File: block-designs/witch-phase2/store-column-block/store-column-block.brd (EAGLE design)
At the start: 27.9 x 27.9 mm, 12 parts, among them IC1 74HC125D

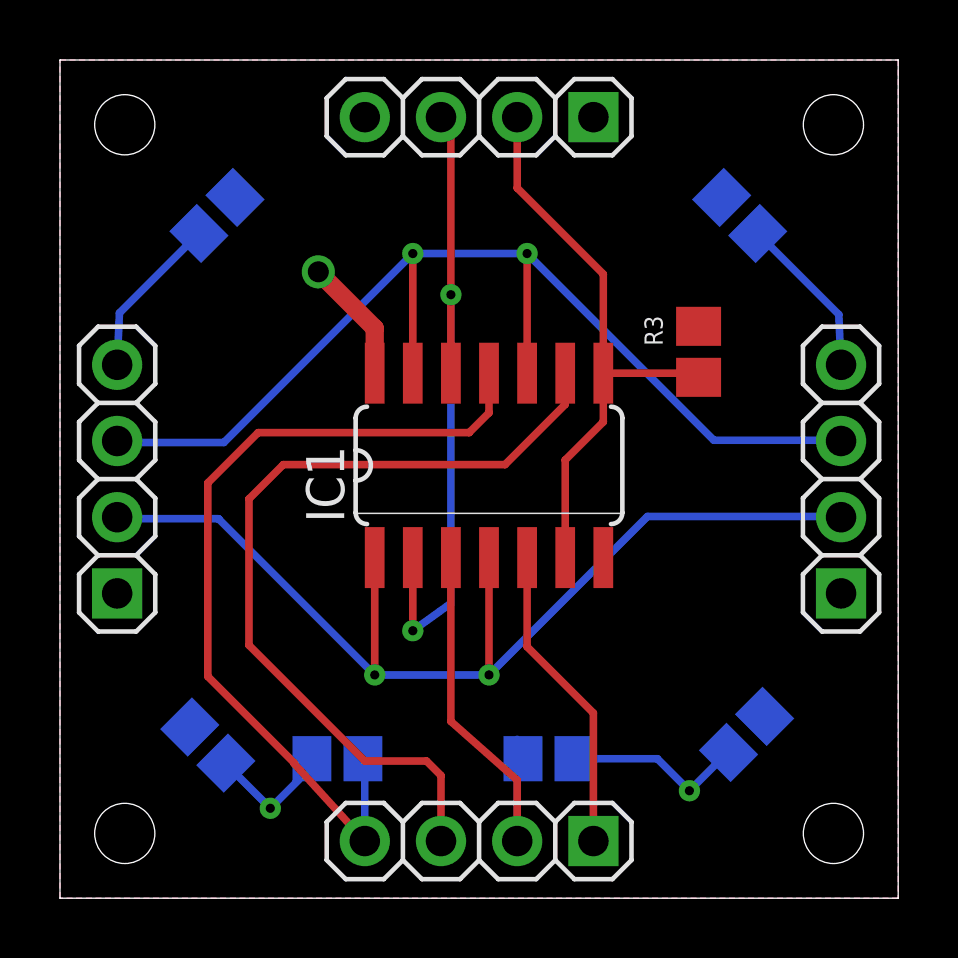
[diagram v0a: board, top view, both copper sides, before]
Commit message: adjust borders for ground/vcc plains and size to match 1.1inch grids
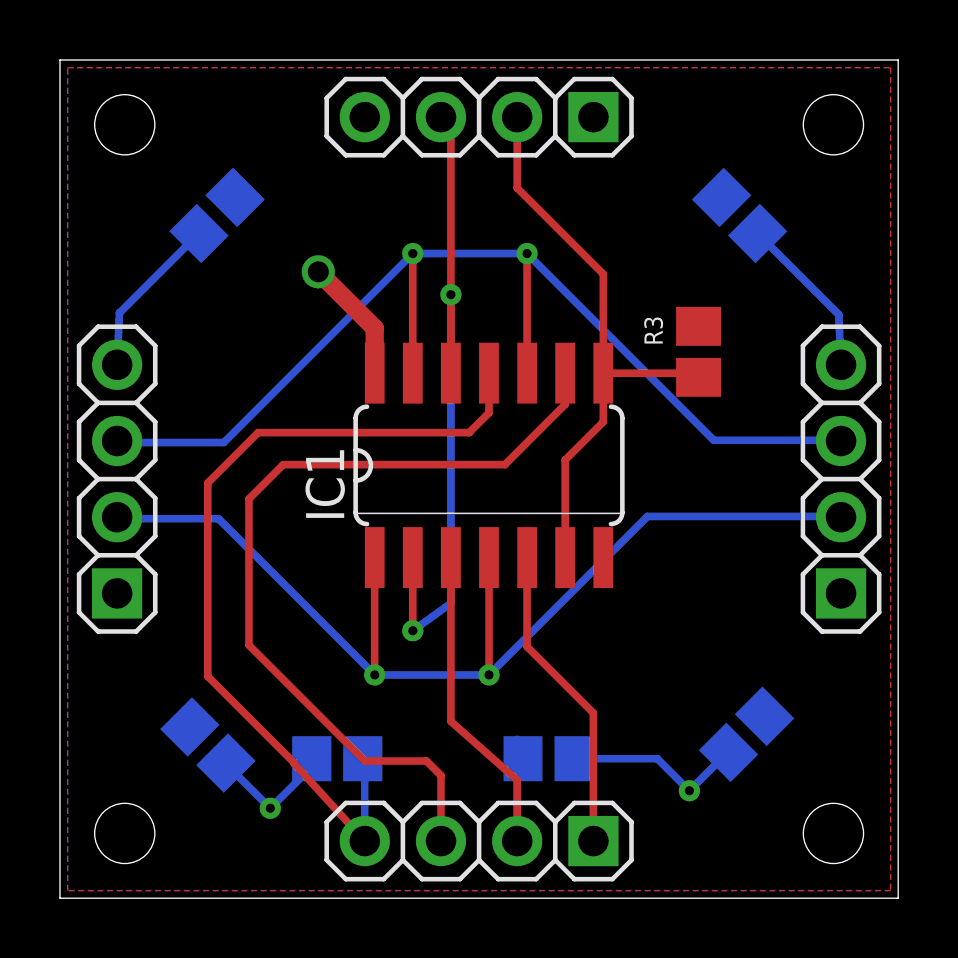
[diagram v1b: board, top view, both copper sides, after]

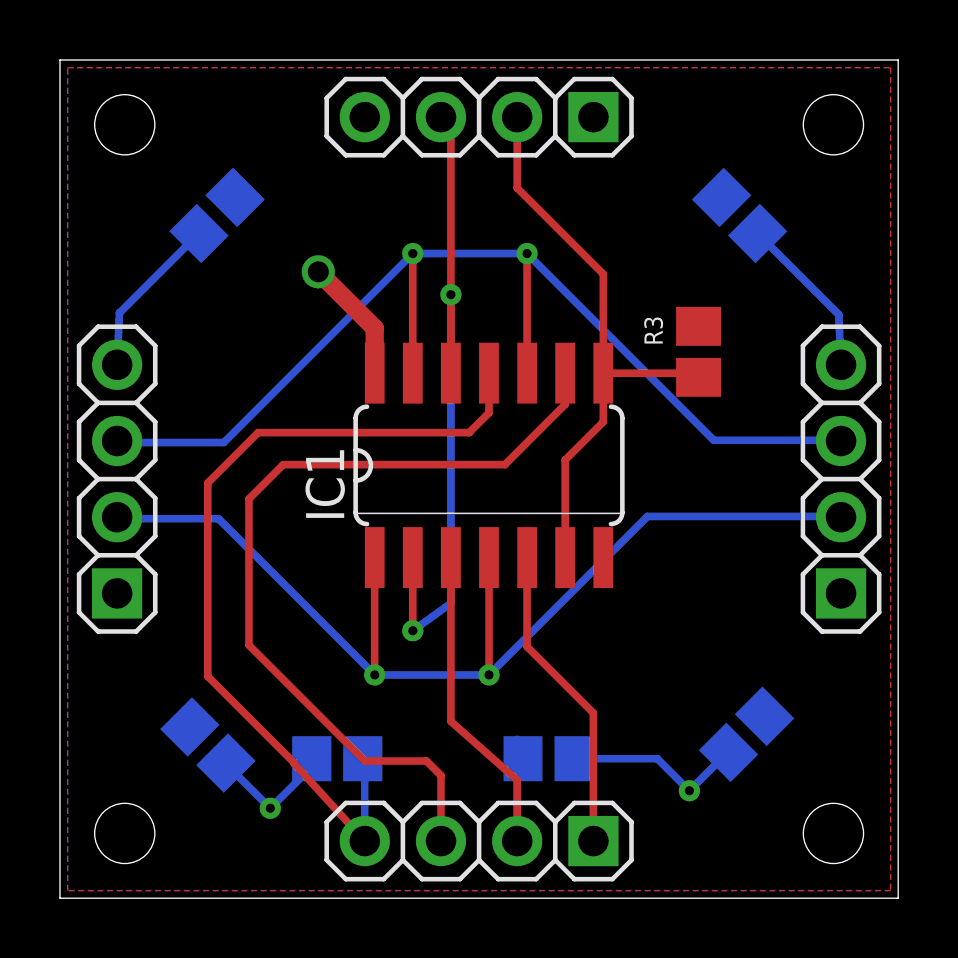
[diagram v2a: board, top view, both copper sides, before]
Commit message: updated designs for new labeling and spacing
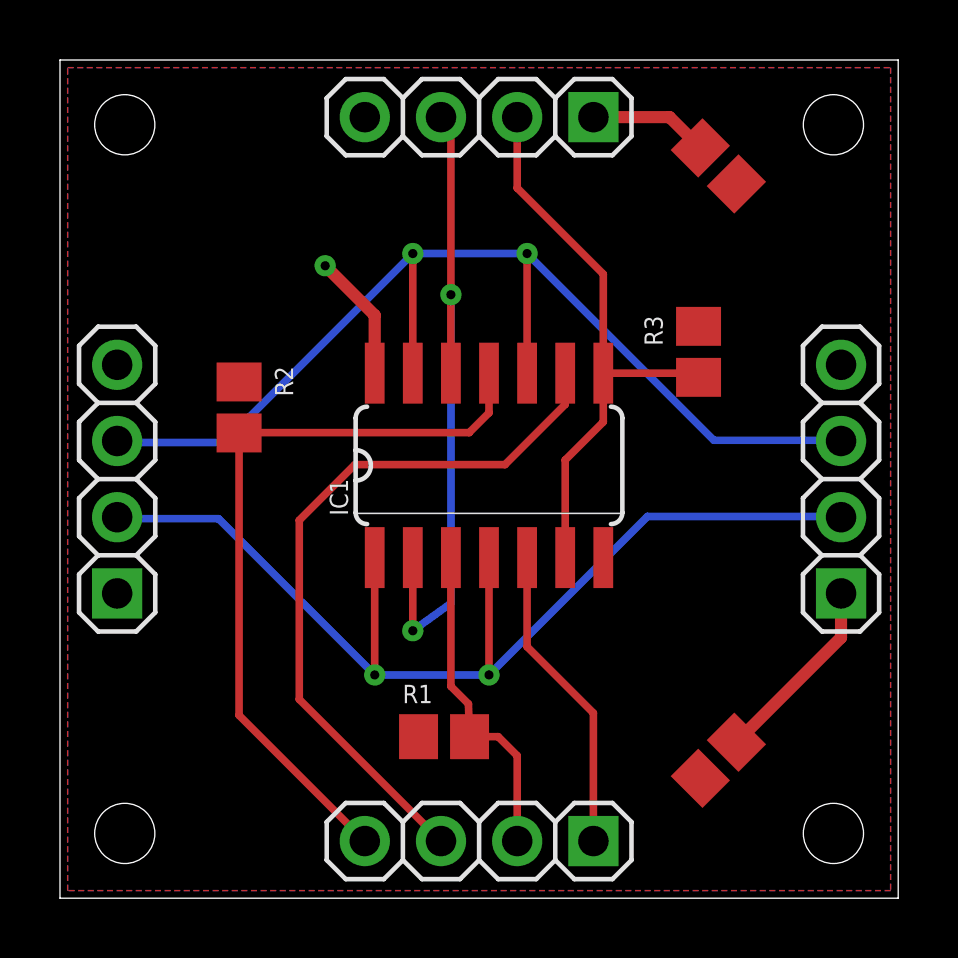
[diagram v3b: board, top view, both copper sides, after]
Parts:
- removed C3, C4: (no value), resistor:C0805
- moved C2 25.7 mm to (21.9, 24.4), flipped to the top, turned to 315 degrees
- moved JP1 17.1 mm to (1.91, 14.0), turned to 90 degrees
- moved JP2 17.1 mm to (14.0, 1.91), turned to 180 degrees
- moved JP3 17.1 mm to (26.0, 14.0), turned to 90 degrees
- moved JP4 17.1 mm to (14.0, 26.0), turned to 180 degrees
- moved R2 12.2 mm to (5.97, 16.4), flipped to the top, turned to 90 degrees
- moved R1 3.56 mm to (12.8, 5.38), flipped to the top
- moved C1 1.28 mm to (21.9, 4.60), flipped to the top, turned to 225 degrees
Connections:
- removed net +5V: C1.1, C2.1, C3.1, C4.1, IC1.14, JP2.1, JP3.1, JP4.1
- new net VCC: C1.1, C2.1, IC1.14, JP1.1, JP3.1, JP4.1
- net CLK: now also JP4.2; no longer JP3.2
- net GND: now also JP1.4; no longer C3.2, C4.2, JP2.4
- net RCV_CLK: now also JP2.3; no longer JP1.3
- net RCV_EN: now also JP1.3, JP3.3; no longer JP2.3, JP4.3
- net RCV_ZC: now also JP2.4; no longer JP1.4
- net SND_CLK: now also JP2.1; no longer JP1.1
- net SND_EN: now also JP1.2, JP3.2; no longer JP2.2, JP4.2
- net SND_ZC: now also JP2.2; no longer JP1.2
- net ZC: now also JP4.3; no longer JP3.3
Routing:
- net GND: track 21.6 -> 0.00 mm, vias 2 -> 0
- net VCC: track 0.00 -> 14.7 mm, vias 0 -> 1
- net +5V: track 4.16 -> 0.00 mm, vias 1 -> 0
- net RCV_CLK: track 28.1 -> 24.2 mm
- net RCV_ZC: track 28.5 -> 25.3 mm
- net SND_ZC: track 13.9 -> 10.9 mm
- added copper zone on layer 16, net VCC
- removed copper zone on layer 16, net +5V
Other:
- board text added: "COL SEL"
- board text removed: "COLUMN SELECT"
- board text removed: "TOP"

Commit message: added caps on the clock lines and switch to 0603 for passives
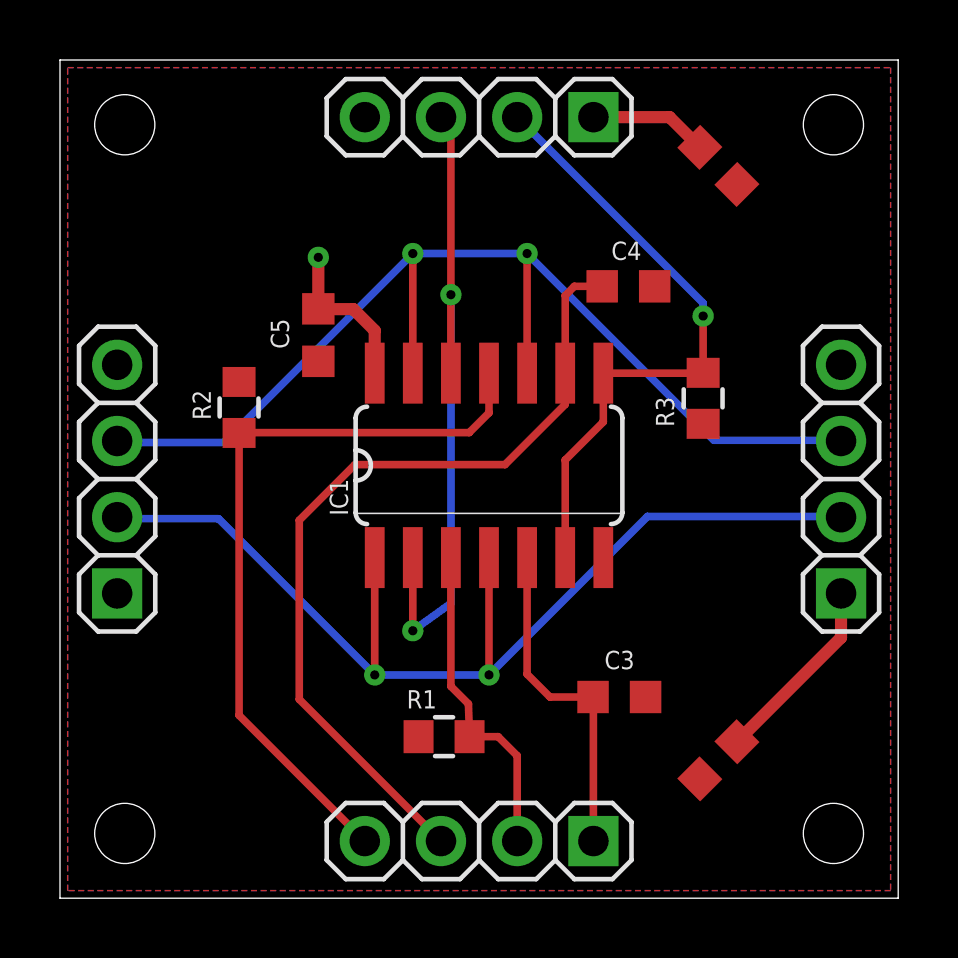
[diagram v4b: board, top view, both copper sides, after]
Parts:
- added C3, C4, C5: (no value), resistor:C0603K
- C1, C2: device resistor:C0805 -> resistor:C0603K
- R1, R2, R3: device resistor:R0805 -> resistor:R0603
- moved R3 1.56 mm to (21.4, 16.7), turned to 270 degrees
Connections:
- net GND: now also C3.2, C4.2, C5.2
- net RCV_CLK: now also C4.1
- net SND_CLK: now also C3.1
- net VCC: now also C5.1
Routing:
- net RCV_CLK: track 24.2 -> 28.1 mm
- net CLK: track 19.6 -> 21.1 mm, vias 0 -> 1
- net VCC: track 14.7 -> 15.7 mm
- net SND_CLK: track 10.4 -> 11.2 mm
